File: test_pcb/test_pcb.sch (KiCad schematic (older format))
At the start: 88 parts, among them K0 KEYSW, K1 KEYSW, K10 KEYSW, K12 KEYSW, K13 KEYSW, K14 KEYSW, K15 KEYSW, K16 KEYSW, K17 KEYSW, K18 KEYSW, K2 KEYSW, K20 KEYSW, K21 KEYSW, K22 KEYSW, K3 KEYSW, K4 KEYSW, K5 KEYSW, K6 KEYSW, K7 KEYSW, K8 KEYSW, K9 KEYSW, P1 CONN_01X15, P10 CONN_01X01, P11 CONN_01X01, P12 CONN_01X01, P13 CONN_01X01, P14 CONN_01X01, P15 CONN_01X01, P2 CONN_01X08, P3 CONN_01X06, P4 CONN_01X01, P5 CONN_01X01, P6 CONN_01X01, P7 CONN_01X01, P8 CONN_01X01, P9 CONN_01X01, U1 STP16CP05

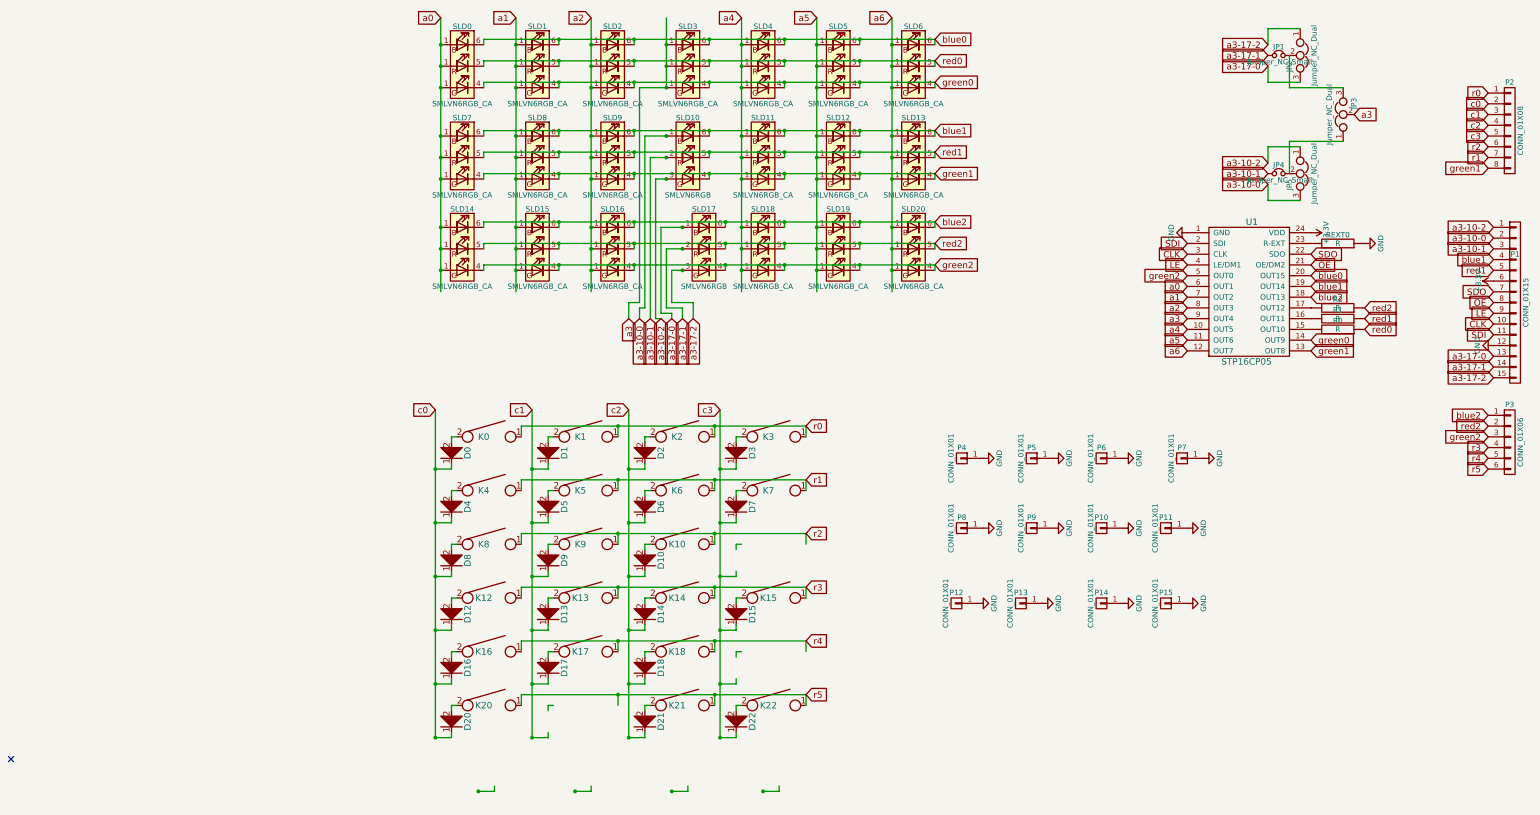
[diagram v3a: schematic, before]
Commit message: test mouting holes and sch cleanup and notes
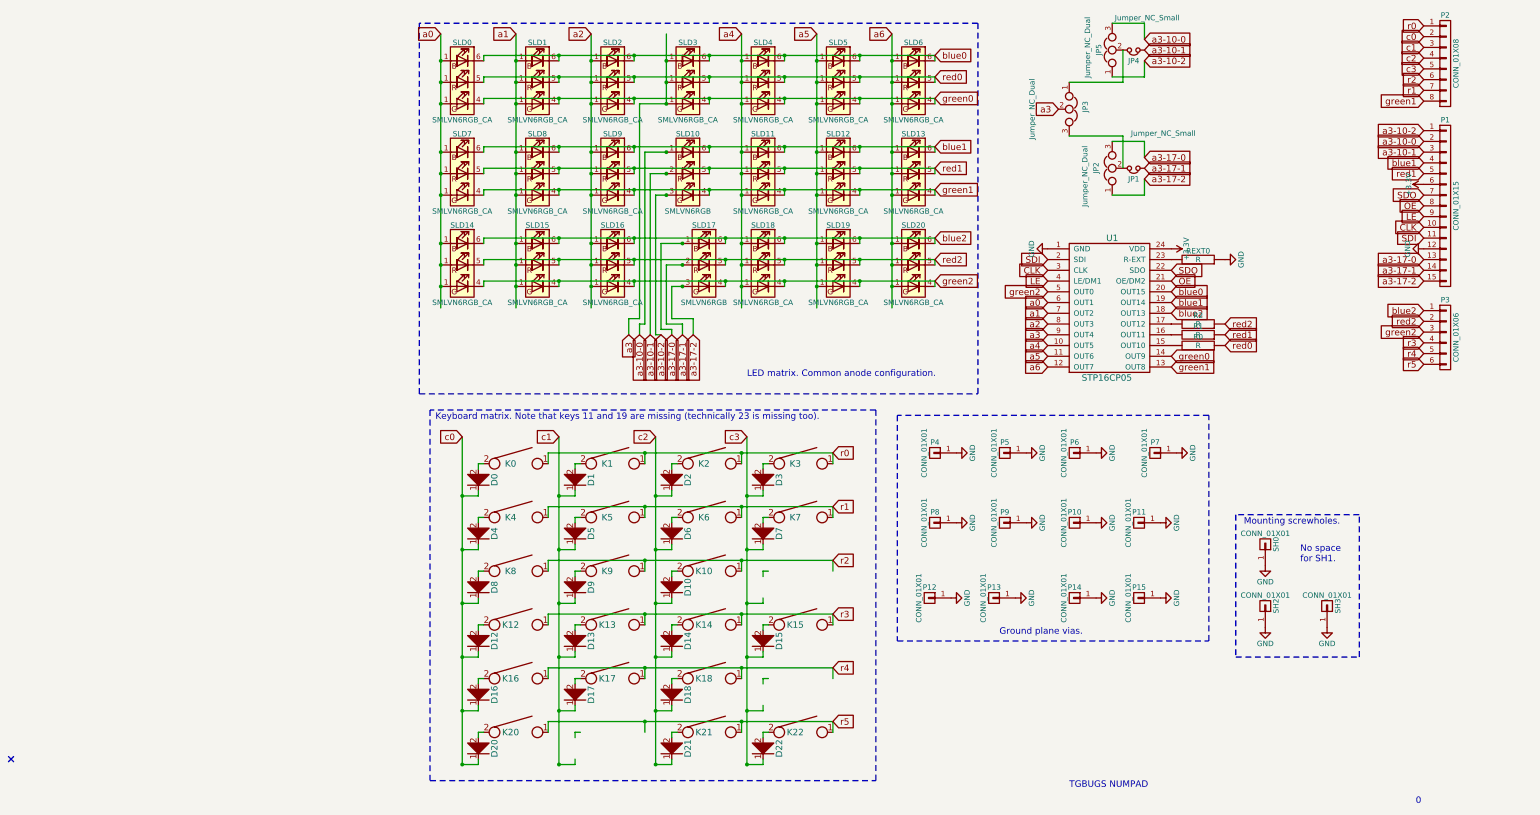
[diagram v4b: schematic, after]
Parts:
- added SH0, SH2, SH3: CONN_01X01, Mounting_Holes:MountingHole_3.2mm_M3_ISO14580_Pad, symbol CONN_01X01
- K7: footprint cherry_rgb:CHERRY_PLATE_150V -> cherry_rgb:CHERRY_PLATE_150V_silkscreen_mod
- R0, R1, R2, REXT0: footprint Resistors_SMD:R_0603_HandSoldering -> cherry_rgb:R_0603_HandSoldering_label_right
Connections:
- wire segments 254 -> 246
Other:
- note added: "0"
- note added: "Ground plane vias."
- note added: "Keyboard matrix. Note that keys 11 and 19 are missing (technically 23 is missing too)."
- note added: "LED matrix. Common anode configuration."
- note added: "Mounting screwholes."
- note added: "No space\nfor SH1."
- note added: "TGBUGS NUMPAD"
- moved on the sheet: D0, D1, D10, D12, D13, D14, D15, D16, D17, D18, D2, D20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

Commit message: test first pass manual routing of anodes for rev 1
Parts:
- removed JP1: Jumper_NC_Small, Pin_Headers:Pin_Header_Angled_1x02_Pitch1.27mm, symbol Jumper_NC_Small
- removed JP2, JP3, JP5: Jumper_NC_Dual, Pin_Headers:Pin_Header_Angled_1x03_Pitch1.27mm, symbol Jumper_NC_Dual
- removed JP4: Jumper_NC_Small, cherry_rgb:Pin_Header_Angled_1x02_Pitch1.27mm_flipped, symbol Jumper_NC_Small
- removed P2: CONN_01X08, Socket_Strips:Socket_Strip_Straight_1x08_Pitch2.54mm, symbol CONN_01X08
- removed P3: CONN_01X06, Socket_Strips:Socket_Strip_Straight_1x06_Pitch2.54mm, symbol CONN_01X06
- added P2: CONN_01X07, Socket_Strips:Socket_Strip_Straight_1x07_Pitch2.54mm, symbol CONN_01X07
- added P3: CONN_01X03, Socket_Strips:Socket_Strip_Straight_1x03_Pitch2.54mm, symbol CONN_01X03
- added Q0, Q1, Q2, Q3: Si3993CDV, TO_SOT_Packages_SMD:SOT-23-6_Handsoldering, symbol Si3993CDV
- added SH1: CONN_01X01, Mounting_Holes:MountingHole_3.2mm_M3_ISO14580_Pad, symbol CONN_01X01
- P1: value CONN_01X15 -> CONN_01X07; footprint Socket_Strips:Socket_Strip_Straight_1x15_Pitch2.54mm -> Socket_Strips:Socket_Strip_Straight_1x07_Pitch2.54mm; symbol CONN_01X15 -> CONN_01X07
- SLD10, SLD17: footprint cherry_rgb:SMLVN6RGB -> cherry_rgb:SMLVN6RGB_CA; symbol SMLVN6RGB -> SMLVN6RGB_CA
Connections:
- net labels added: as0, as1, as2, as3, as4, as5, as6
- wire segments 246 -> 244
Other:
- note removed: "No space\nfor SH1."
- moved on the sheet: R0, R1, R2, REXT0, U1

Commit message: test groundplanes
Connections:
- net labels removed: SDO
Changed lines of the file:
@@
 Text GLabel 9850 3600 0    60   Input ~ 0
 LE
-Text GLabel 9850 3400 0    60   Input ~ 0
-SDO
 Text GLabel 9850 3500 0    60   Input ~ 0
 OE
-Text GLabel 7600 3000 2    60   Input ~ 0
-SDO
 Text GLabel 7600 3100 2    60   Input ~ 0
 OE
@@
 	0    1    -1   0
 $EndComp
+$Comp
+L GND #PWR?
+U 1 1 58C10269
+P 7600 3000
+F 0 "#PWR?" H 7600 2750 50  0001 C CNN
+F 1 "GND" H 7600 2850 50  0000 C CNN
+F 2 "" H 7600 3000 50  0000 C CNN
+F 3 "" H 7600 3000 50  0000 C CNN
+	1    7600 3000
+	0    -1   -1   0
+$EndComp
 $EndSCHEMATC

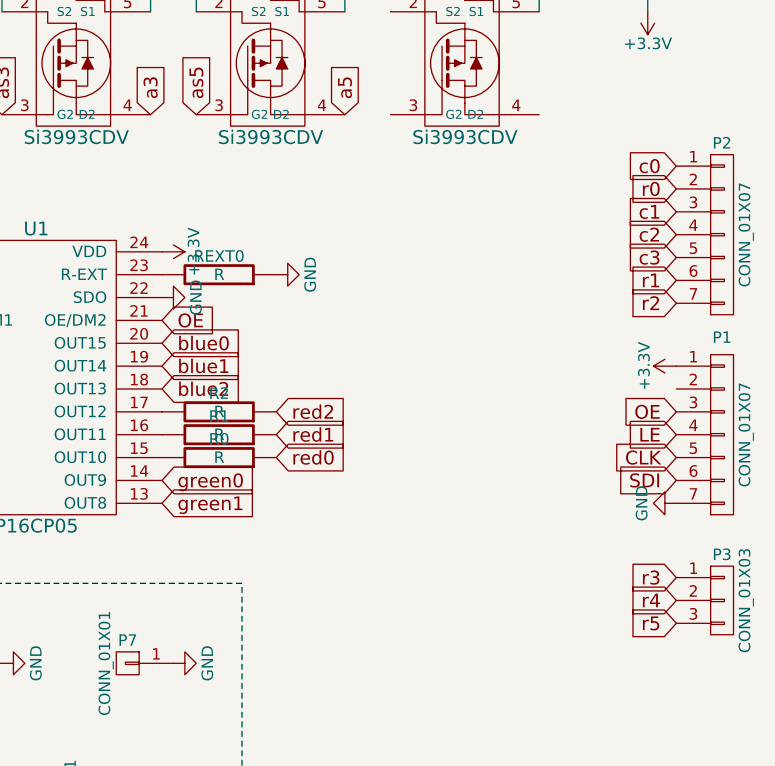
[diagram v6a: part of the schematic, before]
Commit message: test new footprints (the 180 variety) and new design rules
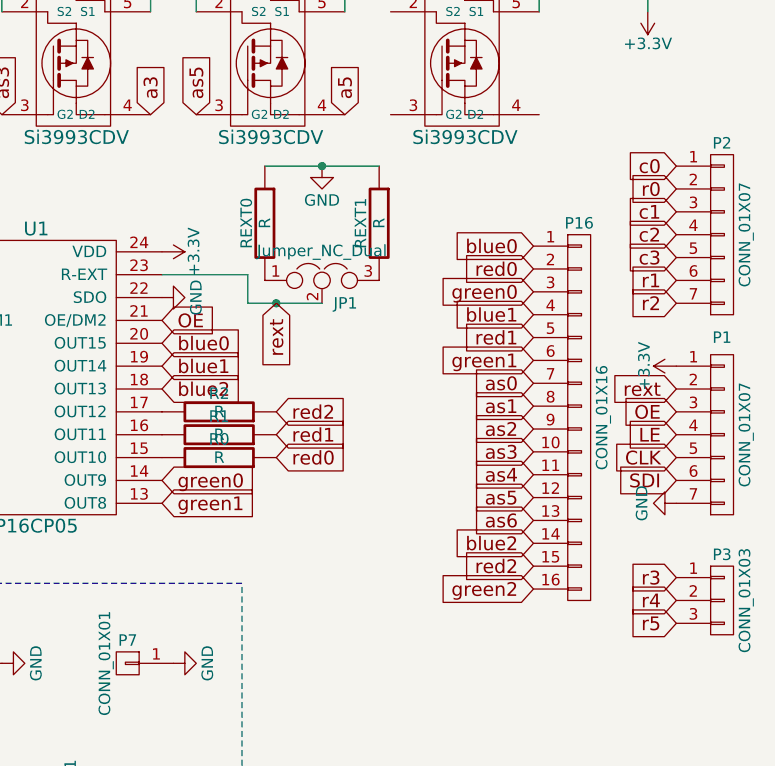
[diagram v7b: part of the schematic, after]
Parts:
- added JP1: Jumper_NC_Dual, Pin_Headers:Pin_Header_Angled_1x03_Pitch1.27mm, symbol Jumper_NC_Dual
- added P16: CONN_01X16, Socket_Strips:Socket_Strip_Straight_1x16_Pitch2.54mm, symbol CONN_01X16
- added REXT1: R, cherry_rgb:R_0603_HandSoldering_label_right, symbol R
- K10, K12, K13, K14, K16, K17, K18, K21, K4, K5, K6, K8, K9: footprint cherry_rgb:CHERRY_PLATE_NH_100H -> cherry_rgb:CHERRY_PLATE_100H
- K7: footprint cherry_rgb:CHERRY_PLATE_150V_silkscreen_mod -> cherry_rgb:CHERRY_PLATE_150V
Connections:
- net labels added: rext
- wire segments 244 -> 248
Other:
- moved on the sheet: REXT0
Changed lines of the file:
@@
 F 0 "K4" H 1450 5200 60  0000 C CNN
 F 1 "KEYSW" H 1500 5100 60  0001 C CNN
-F 2 "cherry_rgb:CHERRY_PLATE_NH_100H" H 1500 5200 60  0001 C CNN
+F 2 "cherry_rgb:CHERRY_PLATE_100H" H 1500 5200 60  0001 C CNN
 F 3 "" H 1500 5200 60  0000 C CNN
 	1    1500 5200
@@
 F 0 "K7" H 4100 5200 60  0000 C CNN
 F 1 "KEYSW" H 4150 5100 60  0001 C CNN
-F 2 "cherry_rgb:CHERRY_PLATE_150V_silkscreen_mod" H 4150 5200 60  0001 C CNN
+F 2 "cherry_rgb:CHERRY_PLATE_150V" H 4150 5200 60  0001 C CNN
 F 3 "" H 4150 5200 60  0000 C CNN
 	1    4150 5200
@@
 F 0 "K5" H 2350 5200 60  0000 C CNN
 F 1 "KEYSW" H 2400 5100 60  0001 C CNN
-F 2 "cherry_rgb:CHERRY_PLATE_NH_100H" H 2400 5200 60  0001 C CNN
+F 2 "cherry_rgb:CHERRY_PLATE_100H" H 2400 5200 60  0001 C CNN
 F 3 "" H 2400 5200 60  0000 C CNN
 	1    2400 5200
@@
 F 0 "K6" H 3250 5200 60  0000 C CNN
 F 1 "KEYSW" H 3300 5100 60  0001 C CNN
-F 2 "cherry_rgb:CHERRY_PLATE_NH_100H" H 3300 5200 60  0001 C CNN
+F 2 "cherry_rgb:CHERRY_PLATE_100H" H 3300 5200 60  0001 C CNN
 F 3 "" H 3300 5200 60  0000 C CNN
 	1    3300 5200
@@
 F 0 "K8" H 1450 5700 60  0000 C CNN
 F 1 "KEYSW" H 1500 5600 60  0001 C CNN
-F 2 "cherry_rgb:CHERRY_PLATE_NH_100H" H 1500 5700 60  0001 C CNN
+F 2 "cherry_rgb:CHERRY_PLATE_100H" H 1500 5700 60  0001 C CNN
 F 3 "" H 1500 5700 60  0000 C CNN
 	1    1500 5700
@@
 F 0 "K9" H 2350 5700 60  0000 C CNN
 F 1 "KEYSW" H 2400 5600 60  0001 C CNN
-F 2 "cherry_rgb:CHERRY_PLATE_NH_100H" H 2400 5700 60  0001 C CNN
+F 2 "cherry_rgb:CHERRY_PLATE_100H" H 2400 5700 60  0001 C CNN
 F 3 "" H 2400 5700 60  0000 C CNN
 	1    2400 5700
@@
 F 0 "K10" H 3250 5700 60  0000 C CNN
 F 1 "KEYSW" H 3300 5600 60  0001 C CNN
-F 2 "cherry_rgb:CHERRY_PLATE_NH_100H" H 3300 5700 60  0001 C CNN
+F 2 "cherry_rgb:CHERRY_PLATE_100H" H 3300 5700 60  0001 C CNN
 F 3 "" H 3300 5700 60  0000 C CNN
 	1    3300 5700
@@
 F 0 "K12" H 1450 6200 60  0000 C CNN
 F 1 "KEYSW" H 1500 6100 60  0001 C CNN
-F 2 "cherry_rgb:CHERRY_PLATE_NH_100H" H 1500 6200 60  0001 C CNN
+F 2 "cherry_rgb:CHERRY_PLATE_100H" H 1500 6200 60  0001 C CNN
 F 3 "" H 1500 6200 60  0000 C CNN
 	1    1500 6200
@@
 F 0 "K13" H 2350 6200 60  0000 C CNN
 F 1 "KEYSW" H 2400 6100 60  0001 C CNN
-F 2 "cherry_rgb:CHERRY_PLATE_NH_100H" H 2400 6200 60  0001 C CNN
+F 2 "cherry_rgb:CHERRY_PLATE_100H" H 2400 6200 60  0001 C CNN
 F 3 "" H 2400 6200 60  0000 C CNN
 	1    2400 6200
@@
 F 0 "K14" H 3250 6200 60  0000 C CNN
 F 1 "KEYSW" H 3300 6100 60  0001 C CNN
-F 2 "cherry_rgb:CHERRY_PLATE_NH_100H" H 3300 6200 60  0001 C CNN
+F 2 "cherry_rgb:CHERRY_PLATE_100H" H 3300 6200 60  0001 C CNN
 F 3 "" H 3300 6200 60  0000 C CNN
 	1    3300 6200
@@
 F 0 "K16" H 1450 6700 60  0000 C CNN
 F 1 "KEYSW" H 1500 6600 60  0001 C CNN
-F 2 "cherry_rgb:CHERRY_PLATE_NH_100H" H 1500 6700 60  0001 C CNN
+F 2 "cherry_rgb:CHERRY_PLATE_100H" H 1500 6700 60  0001 C CNN
 F 3 "" H 1500 6700 60  0000 C CNN
 	1    1500 6700
@@
 F 0 "K17" H 2350 6700 60  0000 C CNN
 F 1 "KEYSW" H 2400 6600 60  0001 C CNN
-F 2 "cherry_rgb:CHERRY_PLATE_NH_100H" H 2400 6700 60  0001 C CNN
+F 2 "cherry_rgb:CHERRY_PLATE_100H" H 2400 6700 60  0001 C CNN
 F 3 "" H 2400 6700 60  0000 C CNN
 	1    2400 6700
@@
 F 0 "K18" H 3250 6700 60  0000 C CNN
 F 1 "KEYSW" H 3300 6600 60  0001 C CNN
-F 2 "cherry_rgb:CHERRY_PLATE_NH_100H" H 3300 6700 60  0001 C CNN
+F 2 "cherry_rgb:CHERRY_PLATE_100H" H 3300 6700 60  0001 C CNN
 F 3 "" H 3300 6700 60  0000 C CNN
 	1    3300 6700
@@
 F 0 "K21" H 3250 7200 60  0000 C CNN
 F 1 "KEYSW" H 3300 7100 60  0001 C CNN
-F 2 "cherry_rgb:CHERRY_PLATE_NH_100H" H 3300 7200 60  0001 C CNN
+F 2 "cherry_rgb:CHERRY_PLATE_100H" H 3300 7200 60  0001 C CNN
 F 3 "" H 3300 7200 60  0000 C CNN
 	1    3300 7200
@@
 L R REXT0
 U 1 1 58BB9157
-P 7850 2900
-F 0 "REXT0" V 7930 2900 50  0000 C CNN
-F 1 "R" V 7850 2900 50  0000 C CNN
-F 2 "cherry_rgb:R_0603_HandSoldering_label_right" H 7850 2900 60  0001 C CNN
-F 3 "" H 7850 2900 60  0000 C CNN
-	1    7850 2900
-	0    1    -1   0
+P 8050 2675
+F 0 "REXT0" V 8130 2675 50  0000 C CNN
+F 1 "R" V 8050 2675 50  0000 C CNN
+F 2 "cherry_rgb:R_0603_HandSoldering_label_right" H 8050 2675 60  0001 C CNN
+F 3 "" H 8050 2675 60  0000 C CNN
+	1    8050 2675
+	-1   0    0    -1
 $EndComp
 $Comp
 L GND #PWR05
 U 1 1 58BB9A32
-P 8100 2900
-F 0 "#PWR05" H 8100 2650 50  0001 C CNN
-F 1 "GND" H 8100 2750 50  0000 C CNN
-F 2 "" H 8100 2900 50  0000 C CNN
-F 3 "" H 8100 2900 50  0000 C CNN
-	1    8100 2900
-	0    -1   -1   0
+P 8300 2425
+F 0 "#PWR05" H 8300 2175 50  0001 C CNN
+F 1 "GND" H 8300 2275 50  0000 C CNN
+F 2 "" H 8300 2425 50  0000 C CNN
+F 3 "" H 8300 2425 50  0000 C CNN
+	1    8300 2425
+	1    0    0    -1
 $EndComp
 $Comp
@@
 $EndComp
 $Comp
-L GND #PWR?
+L GND #PWR023
 U 1 1 58C10269
 P 7600 3000
-F 0 "#PWR?" H 7600 2750 50  0001 C CNN
+F 0 "#PWR023" H 7600 2750 50  0001 C CNN
 F 1 "GND" H 7600 2850 50  0000 C CNN
 F 2 "" H 7600 3000 50  0000 C CNN
@@
 	0    -1   -1   0
 $EndComp
+$Comp
+L CONN_01X16 P16
+U 1 1 58C8D688
+P 9425 3525
+F 0 "P16" H 9425 4375 50  0000 C CNN
+F 1 "CONN_01X16" V 9525 3525 50  0000 C CNN
+F 2 "Socket_Strips:Socket_Strip_Straight_1x16_Pitch2.54mm" H 9425 3525 50  0001 C CNN
+F 3 "" H 9425 3525 50  0000 C CNN
+	1    9425 3525
+	1    0    0    -1
+$EndComp
+Text GLabel 9225 3375 0    60   Input ~ 0
+as0
+Text GLabel 9225 3475 0    60   Input ~ 0
+as1
+Text GLabel 9225 3575 0    60   Input ~ 0
+as2
+Text GLabel 9225 3675 0    60   Input ~ 0
+as3
+Text GLabel 9225 3775 0    60   Input ~ 0
+as4
+Text GLabel 9225 3875 0    60   Input ~ 0
+as5
+Text GLabel 9225 3975 0    60   Input ~ 0
+as6
+Text GLabel 9225 2775 0    60   Input ~ 0
+blue0
+Text GLabel 9225 3075 0    60   Input ~ 0
+blue1
+Text GLabel 9225 4075 0    60   Input ~ 0
+blue2
+Text GLabel 9225 4175 0    60   Input ~ 0
+red2
+Text GLabel 9225 2875 0    60   Input ~ 0
+red0
+Text GLabel 9225 3175 0    60   Input ~ 0
+red1
+Text GLabel 9225 2975 0    60   Input ~ 0
+green0
+Text GLabel 9225 3275 0    60   Input ~ 0
+green1
+Text GLabel 9225 4275 0    60   Input ~ 0
+green2
+$Comp
+L R REXT1
+U 1 1 58C959E3
+P 8550 2675
+F 0 "REXT1" V 8630 2675 50  0000 C CNN
+F 1 "R" V 8550 2675 50  0000 C CNN
+F 2 "cherry_rgb:R_0603_HandSoldering_label_right" H 8550 2675 60  0001 C CNN
+F 3 "" H 8550 2675 60  0000 C CNN
+	1    8550 2675
+	-1   0    0    -1
+$EndComp
+Connection ~ 8300 2425
+$Comp
+L Jumper_NC_Dual JP1
+U 1 1 58C96BCC
+P 8300 2925
+F 0 "JP1" H 8350 2825 50  0000 L CNN
+F 1 "Jumper_NC_Dual" H 8300 3025 50  0000 C BNN
+F 2 "Pin_Headers:Pin_Header_Angled_1x03_Pitch1.27mm" H 8300 2925 50  0001 C CNN
+F 3 "" H 8300 2925 50  0000 C CNN
+	1    8300 2925
+	1    0    0    -1
+$EndComp
+Wire Wire Line
+	8050 2425 8550 2425
+Wire Wire Line
+	7600 2900 7975 2900
+Wire Wire Line
+	7975 2900 7975 3025
+Wire Wire Line
+	7975 3025 8300 3025
+Text GLabel 8100 3025 3    60   Input ~ 0
+rext
+Connection ~ 8100 3025
+Text GLabel 9850 3400 0    60   Input ~ 0
+rext
 $EndSCHEMATC
